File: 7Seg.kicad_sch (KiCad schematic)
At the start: 17 parts, among them Q1 TRANS_PNP-MMBT4403, Q2 TRANS_PNP-MMBT4403, Q3 TRANS_PNP-MMBT4403, Q4 TRANS_PNP-MMBT4403

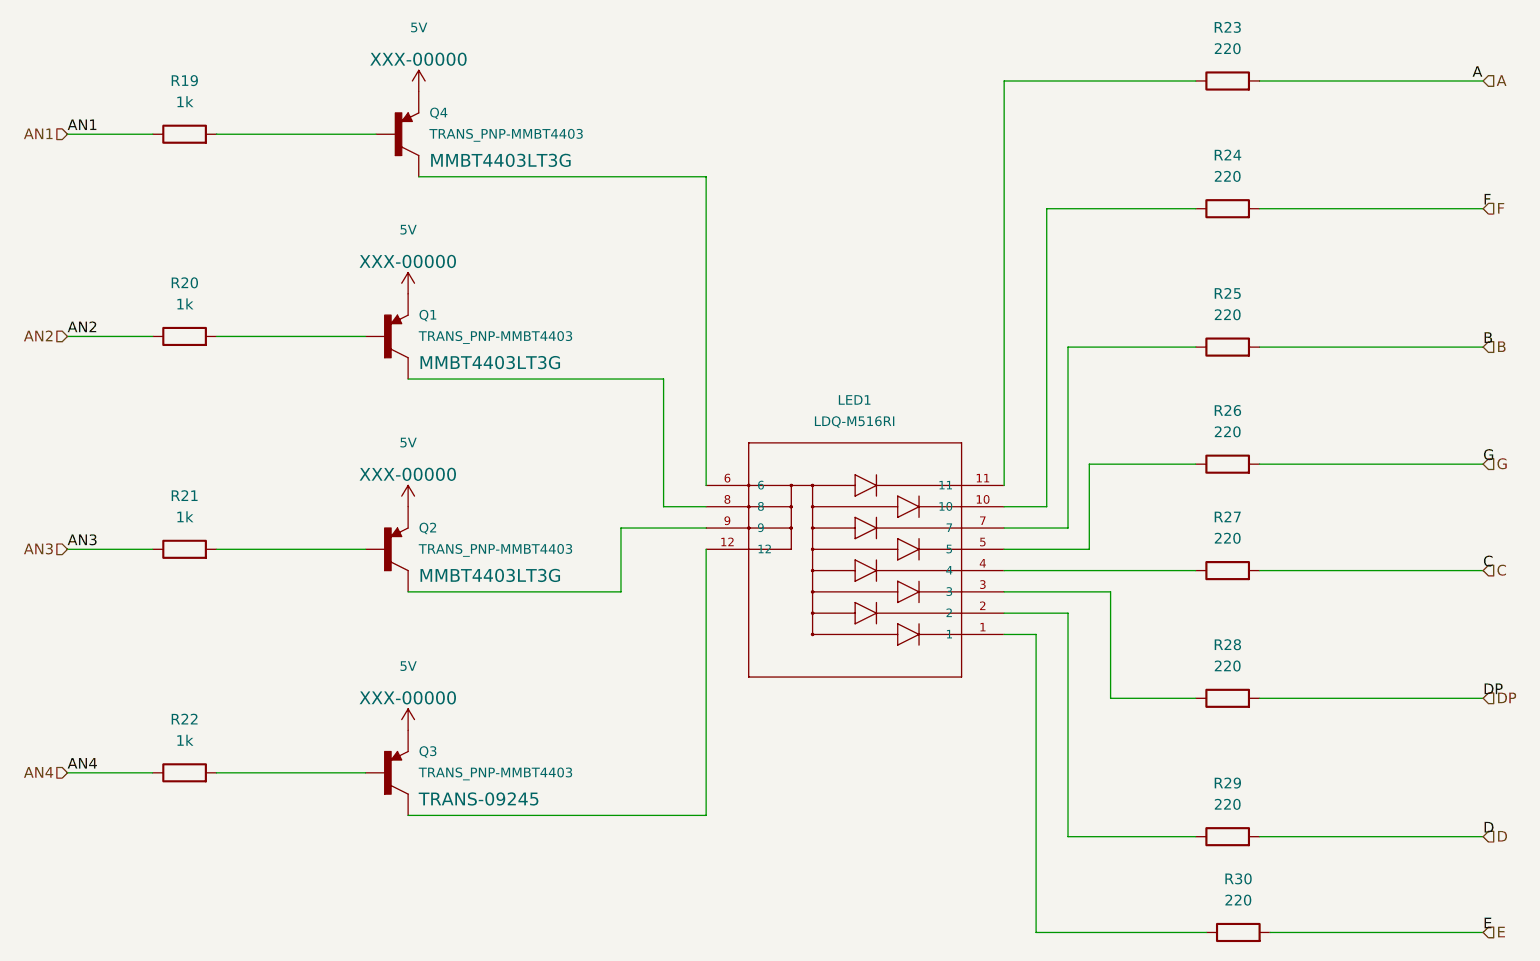
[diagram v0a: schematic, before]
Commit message: First week after winter break. Changed Power circuit design to use different DC to DC converter Setting correct footprints for the components like resistors and capacitors.
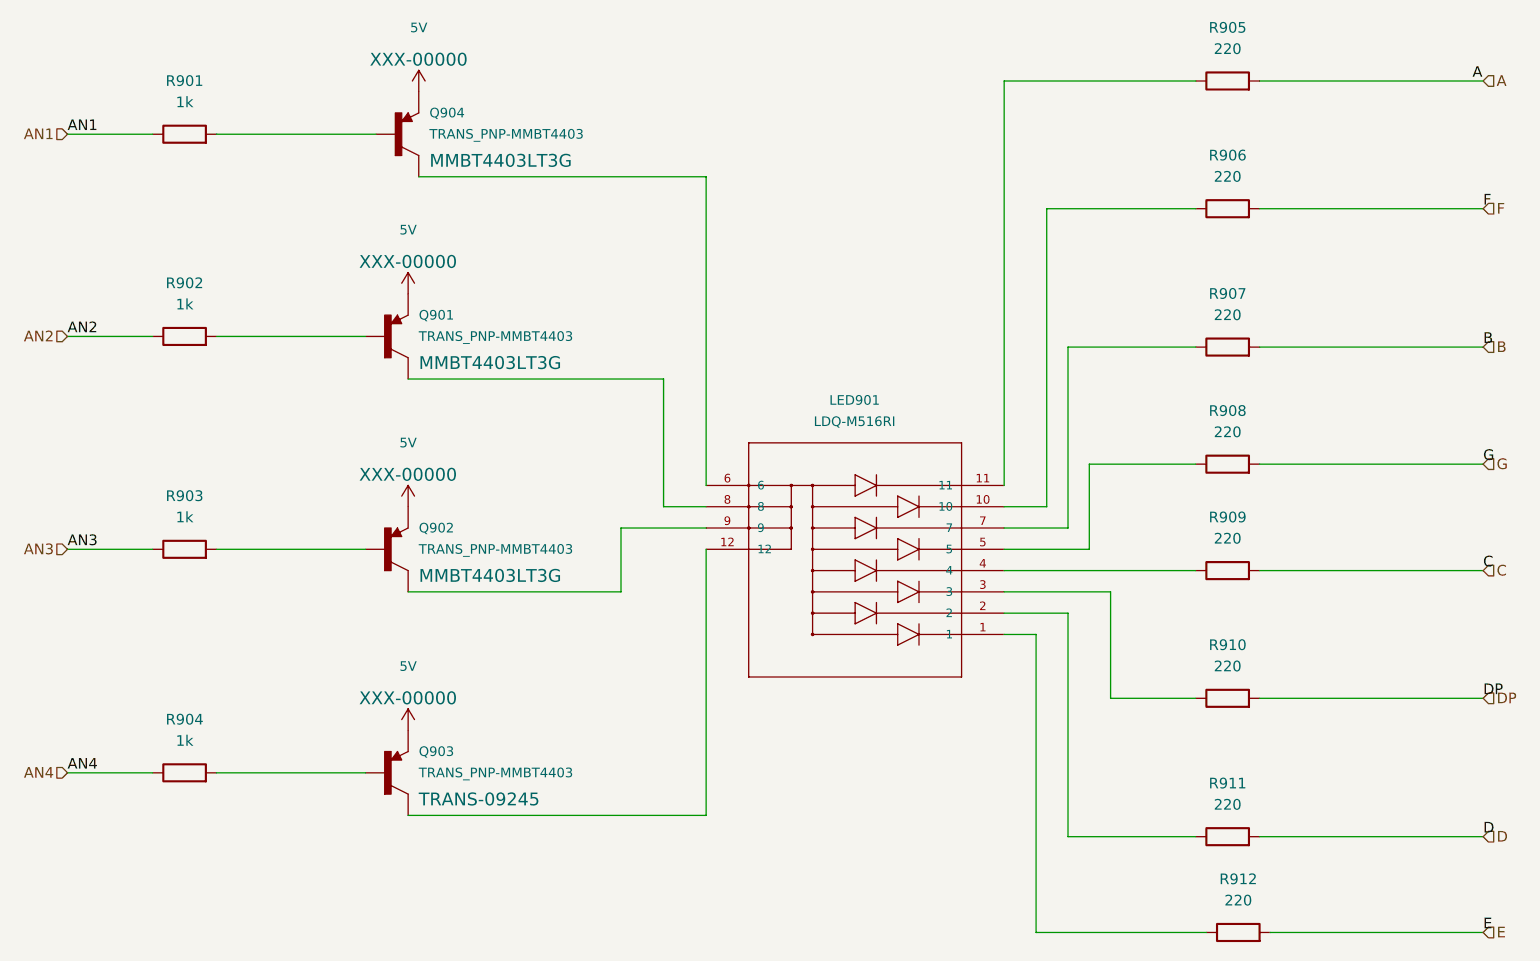
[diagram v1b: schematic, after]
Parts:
- R901: renamed from R19; footprint Resistor_SMD:R_0201_0603Metric -> Resistor_SMD:R_0603_1608Metric; Manufacturer_Name (none) -> UNI-ROYAL(Uniroyal Elec); Manufacturer_Part_Number (none) -> 0603WAF1001T5E
- R902: renamed from R20; footprint Resistor_SMD:R_0201_0603Metric -> Resistor_SMD:R_0603_1608Metric; Manufacturer_Name (none) -> UNI-ROYAL(Uniroyal Elec); Manufacturer_Part_Number (none) -> 0603WAF1001T5E
- R903: renamed from R21; footprint Resistor_SMD:R_0201_0603Metric -> Resistor_SMD:R_0603_1608Metric; Manufacturer_Name (none) -> UNI-ROYAL(Uniroyal Elec); Manufacturer_Part_Number (none) -> 0603WAF1001T5E
- R904: renamed from R22; footprint Resistor_SMD:R_0201_0603Metric -> Resistor_SMD:R_0603_1608Metric; Manufacturer_Name (none) -> UNI-ROYAL(Uniroyal Elec); Manufacturer_Part_Number (none) -> 0603WAF1001T5E
- R905: renamed from R23; footprint Resistor_SMD:R_0201_0603Metric -> Resistor_SMD:R_0603_1608Metric; Manufacturer_Name (none) -> UNI-ROYAL(Uniroyal Elec); Manufacturer_Part_Number (none) -> 0603WAF2200T5E
- R906: renamed from R24; footprint Resistor_SMD:R_0201_0603Metric -> Resistor_SMD:R_0603_1608Metric; Manufacturer_Name (none) -> UNI-ROYAL(Uniroyal Elec); Manufacturer_Part_Number (none) -> 0603WAF2200T5E
- R907: renamed from R25; footprint Resistor_SMD:R_0201_0603Metric -> Resistor_SMD:R_0603_1608Metric; Manufacturer_Name (none) -> UNI-ROYAL(Uniroyal Elec); Manufacturer_Part_Number (none) -> 0603WAF2200T5E
- R908: renamed from R26; footprint Resistor_SMD:R_0201_0603Metric -> Resistor_SMD:R_0603_1608Metric; Manufacturer_Name (none) -> UNI-ROYAL(Uniroyal Elec); Manufacturer_Part_Number (none) -> 0603WAF2200T5E
- R909: renamed from R27; footprint Resistor_SMD:R_0201_0603Metric -> Resistor_SMD:R_0603_1608Metric; Manufacturer_Name (none) -> UNI-ROYAL(Uniroyal Elec); Manufacturer_Part_Number (none) -> 0603WAF2200T5E
- R910: renamed from R28; footprint Resistor_SMD:R_0201_0603Metric -> Resistor_SMD:R_0603_1608Metric; Manufacturer_Name (none) -> UNI-ROYAL(Uniroyal Elec); Manufacturer_Part_Number (none) -> 0603WAF2200T5E
- R911: renamed from R29; footprint Resistor_SMD:R_0201_0603Metric -> Resistor_SMD:R_0603_1608Metric; Manufacturer_Name (none) -> UNI-ROYAL(Uniroyal Elec); Manufacturer_Part_Number (none) -> 0603WAF2200T5E
- R912: renamed from R30; footprint Resistor_SMD:R_0201_0603Metric -> Resistor_SMD:R_0603_1608Metric; Manufacturer_Name (none) -> UNI-ROYAL(Uniroyal Elec); Manufacturer_Part_Number (none) -> 0603WAF2200T5E
- renumbered LED1 to LED901, Q1 to Q901, Q2 to Q902, Q3 to Q903, Q4 to Q904

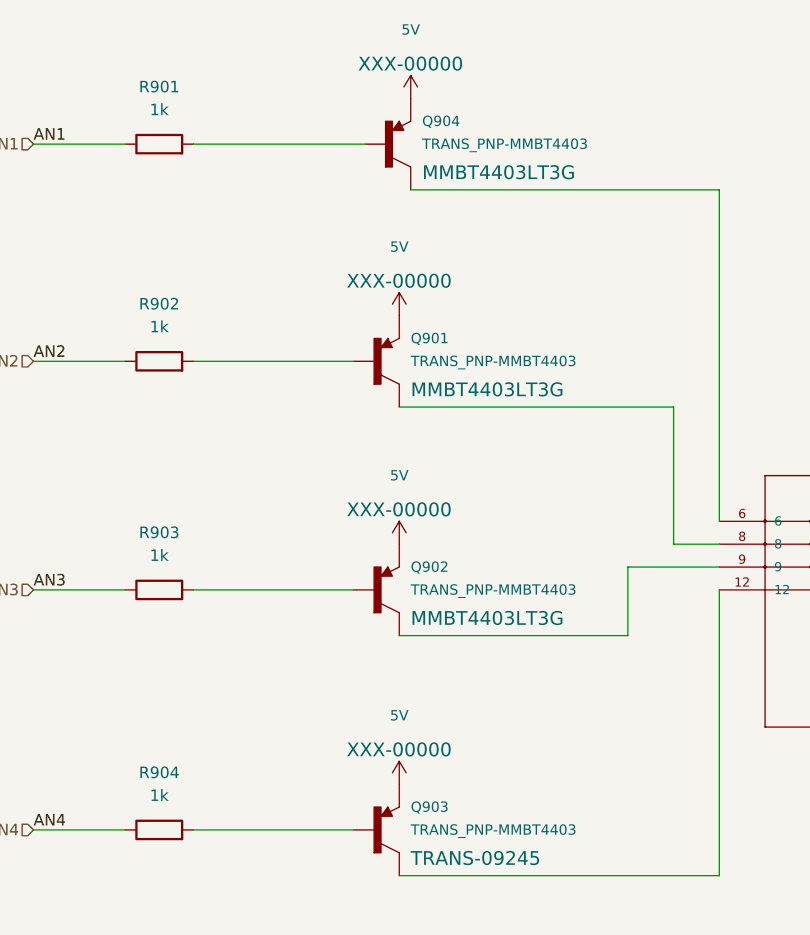
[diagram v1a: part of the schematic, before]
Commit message: Weekend progress
Things that remain:
4 LEDs to Microcontroller
7-Seg to Microcontroller
LCD to Microcontroller
Microphone and Speakers to Microcontroller
Power circuitry
USB-C connector
Reset and Boot buttons
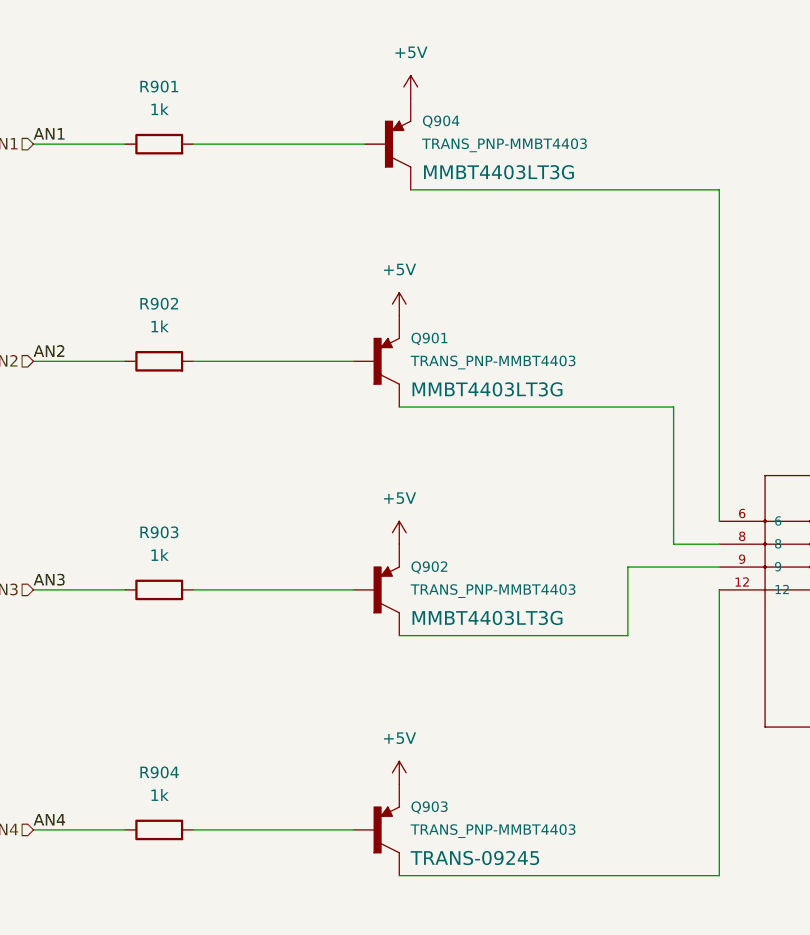
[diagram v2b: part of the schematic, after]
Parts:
- Q901, Q902, Q903, Q904: footprint Custom:MMBT4403LT3G -> Package_TO_SOT_SMD:SOT-23
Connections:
- net 5V renamed +5V
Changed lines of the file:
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@@
     (pin "9")
-  )
-  (symbol (lib_id "SparkFun-PowerSymbols:5V") (at 92.71 124.46 0) (unit 1)
-    (in_bom yes) (on_board yes) (fields_autoplaced)
-    (property "Reference" "#SUPPLY0903" (id 0) (at 93.98 124.46 0)
-      (effects (font (size 1.143 1.143)) (justify left bottom) hide)
-    )
-    (property "Value" "5V" (id 1) (at 92.71 116.84 0)
-      (effects (font (size 1.143 1.143)))
-    )
-    (property "Footprint" "XXX-00000" (id 2) (at 92.71 120.65 0)
-      (effects (font (size 1.524 1.524)))
-    )
-    (property "Datasheet" "" (id 3) (at 92.71 124.46 0)
-      (effects (font (size 1.524 1.524)) hide)
-    )
-    (pin "~")
   )
   (symbol (lib_id "Device:R") (at 191.77 148.59 90) (unit 1)
@@
     (pin "2")
   )
+  (symbol (lib_id "power:+5V") (at 92.71 124.46 0) (unit 1)
+    (in_bom yes) (on_board yes) (fields_autoplaced)
+    (property "Reference" "#PWR0903" (id 0) (at 92.71 128.27 0)
+      (effects (font (size 1.27 1.27)) hide)
+    )
+    (property "Value" "+5V" (id 1) (at 92.71 119.38 0))
+    (property "Footprint" "" (id 2) (at 92.71 124.46 0)
+      (effects (font (size 1.27 1.27)) hide)
+    )
+    (property "Datasheet" "" (id 3) (at 92.71 124.46 0)
+      (effects (font (size 1.27 1.27)) hide)
+    )
+    (pin "1")
+  )
   (symbol (lib_id "SparkFun-DiscreteSemi:TRANS_PNP-MMBT4403") (at 91.44 53.34 0) (unit 1)
     (in_bom yes) (on_board yes) (fields_autoplaced)
@@
       (effects (font (size 1.143 1.143)) (justify left))
     )
-    (property "Footprint" "Custom:MMBT4403LT3G" (id 2) (at 91.44 46.99 0)
+    (property "Footprint" "Package_TO_SOT_SMD:SOT-23" (id 2) (at 91.44 46.99 0)
       (effects (font (size 0.508 0.508)) hide)
     )
@@
     (pin "2")
   )
-  (symbol (lib_id "SparkFun-PowerSymbols:5V") (at 92.71 72.39 0) (unit 1)
-    (in_bom yes) (on_board yes) (fields_autoplaced)
-    (property "Reference" "#SUPPLY0901" (id 0) (at 93.98 72.39 0)
-      (effects (font (size 1.143 1.143)) (justify left bottom) hide)
-    )
-    (property "Value" "5V" (id 1) (at 92.71 64.77 0)
-      (effects (font (size 1.143 1.143)))
-    )
-    (property "Footprint" "XXX-00000" (id 2) (at 92.71 68.58 0)
-      (effects (font (size 1.524 1.524)))
-    )
-    (property "Datasheet" "" (id 3) (at 92.71 72.39 0)
-      (effects (font (size 1.524 1.524)) hide)
-    )
-    (pin "~")
-  )
   (symbol (lib_id "Device:R") (at 66.04 77.47 90) (unit 1)
     (in_bom yes) (on_board yes) (fields_autoplaced)
@@
     (pin "2")
   )
-  (symbol (lib_id "SparkFun-PowerSymbols:5V") (at 93.98 48.26 0) (unit 1)
-    (in_bom yes) (on_board yes) (fields_autoplaced)
-    (property "Reference" "#SUPPLY0904" (id 0) (at 95.25 48.26 0)
-      (effects (font (size 1.143 1.143)) (justify left bottom) hide)
-    )
-    (property "Value" "5V" (id 1) (at 93.98 40.64 0)
-      (effects (font (size 1.143 1.143)))
-    )
-    (property "Footprint" "XXX-00000" (id 2) (at 93.98 44.45 0)
-      (effects (font (size 1.524 1.524)))
-    )
-    (property "Datasheet" "" (id 3) (at 93.98 48.26 0)
-      (effects (font (size 1.524 1.524)) hide)
-    )
-    (pin "~")
-  )
   (symbol (lib_id "Device:R") (at 190.5 78.74 90) (unit 1)
     (in_bom yes) (on_board yes) (fields_autoplaced)
@@
       (effects (font (size 1.143 1.143)) (justify left))
     )
-    (property "Footprint" "Custom:MMBT4403LT3G" (id 2) (at 90.17 123.19 0)
+    (property "Footprint" "Package_TO_SOT_SMD:SOT-23" (id 2) (at 90.17 123.19 0)
       (effects (font (size 0.508 0.508)) hide)
     )
@@
     (pin "2")
     (pin "3")
+  )
+  (symbol (lib_id "power:+5V") (at 93.98 48.26 0) (unit 1)
+    (in_bom yes) (on_board yes) (fields_autoplaced)
+    (property "Reference" "#PWR0904" (id 0) (at 93.98 52.07 0)
+      (effects (font (size 1.27 1.27)) hide)
+    )
+    (property "Value" "+5V" (id 1) (at 93.98 43.18 0))
+    (property "Footprint" "" (id 2) (at 93.98 48.26 0)
+      (effects (font (size 1.27 1.27)) hide)
+    )
+    (property "Datasheet" "" (id 3) (at 93.98 48.26 0)
+      (effects (font (size 1.27 1.27)) hide)
+    )
+    (pin "1")
   )
   (symbol (lib_id "Device:R") (at 66.04 129.54 90) (unit 1)
@@
       (effects (font (size 1.143 1.143)) (justify left))
     )
-    (property "Footprint" "Custom:MMBT4403LT3G" (id 2) (at 90.17 96.52 0)
+    (property "Footprint" "Package_TO_SOT_SMD:SOT-23" (id 2) (at 90.17 96.52 0)
       (effects (font (size 0.508 0.508)) hide)
     )
@@
     (pin "3")
   )
-  (symbol (lib_id "SparkFun-PowerSymbols:5V") (at 92.71 97.79 0) (unit 1)
-    (in_bom yes) (on_board yes) (fields_autoplaced)
-    (property "Reference" "#SUPPLY0902" (id 0) (at 93.98 97.79 0)
-      (effects (font (size 1.143 1.143)) (justify left bottom) hide)
-    )
-    (property "Value" "5V" (id 1) (at 92.71 90.17 0)
-      (effects (font (size 1.143 1.143)))
-    )
-    (property "Footprint" "XXX-00000" (id 2) (at 92.71 93.98 0)
-      (effects (font (size 1.524 1.524)))
-    )
-    (property "Datasheet" "" (id 3) (at 92.71 97.79 0)
-      (effects (font (size 1.524 1.524)) hide)
-    )
-    (pin "~")
+  (symbol (lib_id "power:+5V") (at 92.71 72.39 0) (unit 1)
+    (in_bom yes) (on_board yes) (fields_autoplaced)
+    (property "Reference" "#PWR0901" (id 0) (at 92.71 76.2 0)
+      (effects (font (size 1.27 1.27)) hide)
+    )
+    (property "Value" "+5V" (id 1) (at 92.71 67.31 0))
+    (property "Footprint" "" (id 2) (at 92.71 72.39 0)
+      (effects (font (size 1.27 1.27)) hide)
+    )
+    (property "Datasheet" "" (id 3) (at 92.71 72.39 0)
+      (effects (font (size 1.27 1.27)) hide)
+    )
+    (pin "1")
   )
   (symbol (lib_id "Device:R") (at 190.5 62.23 90) (unit 1)
@@
       (effects (font (size 1.143 1.143)) (justify left))
     )
-    (property "Footprint" "Custom:MMBT4403LT3G" (id 2) (at 90.17 71.12 0)
+    (property "Footprint" "Package_TO_SOT_SMD:SOT-23" (id 2) (at 90.17 71.12 0)
       (effects (font (size 0.508 0.508)) hide)
     )
@@
     (pin "3")
   )
+  (symbol (lib_id "power:+5V") (at 92.71 97.79 0) (unit 1)
+    (in_bom yes) (on_board yes) (fields_autoplaced)
+    (property "Reference" "#PWR0902" (id 0) (at 92.71 101.6 0)
+      (effects (font (size 1.27 1.27)) hide)
+    )
+    (property "Value" "+5V" (id 1) (at 92.71 92.71 0))
+    (property "Footprint" "" (id 2) (at 92.71 97.79 0)
+      (effects (font (size 1.27 1.27)) hide)
+    )
+    (property "Datasheet" "" (id 3) (at 92.71 97.79 0)
+      (effects (font (size 1.27 1.27)) hide)
+    )
+    (pin "1")
+  )
   (symbol (lib_id "Device:R") (at 190.5 120.65 90) (unit 1)

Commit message: Update BOM and POC files
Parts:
- LED901: Manufacturer_Name (none) -> Lumex Opto/Components Inc.; Manufacturer_Part_Number (none) -> 67-1449-ND
- Q901, Q902, Q903, Q904: value TRANS_PNP-MMBT4403 -> SMMBT4403LT1G; Manufacturer_Name (none) -> onsemi; Manufacturer_Part_Number (none) -> SMMBT4403LT1G
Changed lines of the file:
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@@
+      (effects (font (size 1.27 1.27)) hide)
+    )
+    (property "Manufacturer_Name" "Lumex Opto/Components Inc." (id 4) (at 125.73 95.25 0)
+      (effects (font (size 1.27 1.27)) hide)
+    )
+    (property "Manufacturer_Part_Number" "67-1449-ND" (id 5) (at 125.73 95.25 0)
       (effects (font (size 1.27 1.27)) hide)
     )
@@
       (effects (font (size 1.143 1.143)) (justify left))
     )
-    (property "Value" "TRANS_PNP-MMBT4403" (id 1) (at 95.25 53.34 0)
+    (property "Value" "SMMBT4403LT1G" (id 1) (at 95.25 53.34 0)
       (effects (font (size 1.143 1.143)) (justify left))
     )
@@
     (property "Field4" "MMBT4403LT3G" (id 4) (at 95.25 56.515 0)
       (effects (font (size 1.524 1.524)) (justify left))
+    )
+    (property "Manufacturer_Name" "onsemi" (id 5) (at 91.44 53.34 0)
+      (effects (font (size 1.27 1.27)) hide)
+    )
+    (property "Manufacturer_Part_Number" "SMMBT4403LT1G" (id 6) (at 91.44 53.34 0)
+      (effects (font (size 1.27 1.27)) hide)
     )
     (pin "1")
@@
       (effects (font (size 1.143 1.143)) (justify left))
     )
-    (property "Value" "TRANS_PNP-MMBT4403" (id 1) (at 93.98 129.54 0)
+    (property "Value" "SMMBT4403LT1G" (id 1) (at 93.98 129.54 0)
       (effects (font (size 1.143 1.143)) (justify left))
     )
@@
     (property "Field4" "TRANS-09245" (id 4) (at 93.98 132.715 0)
       (effects (font (size 1.524 1.524)) (justify left))
+    )
+    (property "Manufacturer_Name" "onsemi" (id 5) (at 90.17 129.54 0)
+      (effects (font (size 1.27 1.27)) hide)
+    )
+    (property "Manufacturer_Part_Number" "SMMBT4403LT1G" (id 6) (at 90.17 129.54 0)
+      (effects (font (size 1.27 1.27)) hide)
     )
     (pin "1")
@@
       (effects (font (size 1.143 1.143)) (justify left))
     )
-    (property "Value" "TRANS_PNP-MMBT4403" (id 1) (at 93.98 102.87 0)
+    (property "Value" "SMMBT4403LT1G" (id 1) (at 93.98 102.87 0)
       (effects (font (size 1.143 1.143)) (justify left))
     )
@@
     (property "Field4" "MMBT4403LT3G" (id 4) (at 93.98 106.045 0)
       (effects (font (size 1.524 1.524)) (justify left))
+    )
+    (property "Manufacturer_Name" "onsemi" (id 5) (at 90.17 102.87 0)
+      (effects (font (size 1.27 1.27)) hide)
+    )
+    (property "Manufacturer_Part_Number" "SMMBT4403LT1G" (id 6) (at 90.17 102.87 0)
+      (effects (font (size 1.27 1.27)) hide)
     )
     (pin "1")
@@
       (effects (font (size 1.143 1.143)) (justify left))
     )
-    (property "Value" "TRANS_PNP-MMBT4403" (id 1) (at 93.98 77.47 0)
+    (property "Value" "SMMBT4403LT1G" (id 1) (at 93.98 77.47 0)
       (effects (font (size 1.143 1.143)) (justify left))
     )
@@
       (effects (font (size 1.524 1.524)) (justify left))
     )
-    (pin "1")
+    (property "Manufacturer_Name" "onsemi" (id 5) (at 90.17 77.47 0)
+      (effects (font (size 1.27 1.27)) hide)
+    )
+    (property "Manufacturer_Part_Number" "SMMBT4403LT1G" (id 6) (at 90.17 77.47 0)
+      (effects (font (size 1.27 1.27)) hide)
+    )
+    (pin "1")
